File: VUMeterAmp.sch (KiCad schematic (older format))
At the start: 61 parts, among them J1 Conn_01x03, J2 Conn_01x03, J3 Conn_01x07, J4 Conn_01x07, J5 Conn_01x03, SW1 SW_DPST_x2, U1 NJM4580, U2 NJM4580

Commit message: add gbr
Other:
- note added: "+0.4V"
- note added: "-0.4V"
- note added: "4.7k"
- note added: "7.43k\n---\n2.57k"
- note added: "peak cut ±1V"
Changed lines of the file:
@@
 	1    0    0    -1
 $EndComp
+Text Notes 4625 3450 0    50   ~ 0
+7.43k\n---\n2.57k
+Text Notes 7800 3450 0    50   ~ 0
+4.7k
+Text Notes 1950 5275 0    50   ~ 0
+peak cut ±1V
+Text Notes 2175 5850 0    50   ~ 0
++0.4V
+Text Notes 3350 5850 0    50   ~ 0
+-0.4V
 $EndSCHEMATC

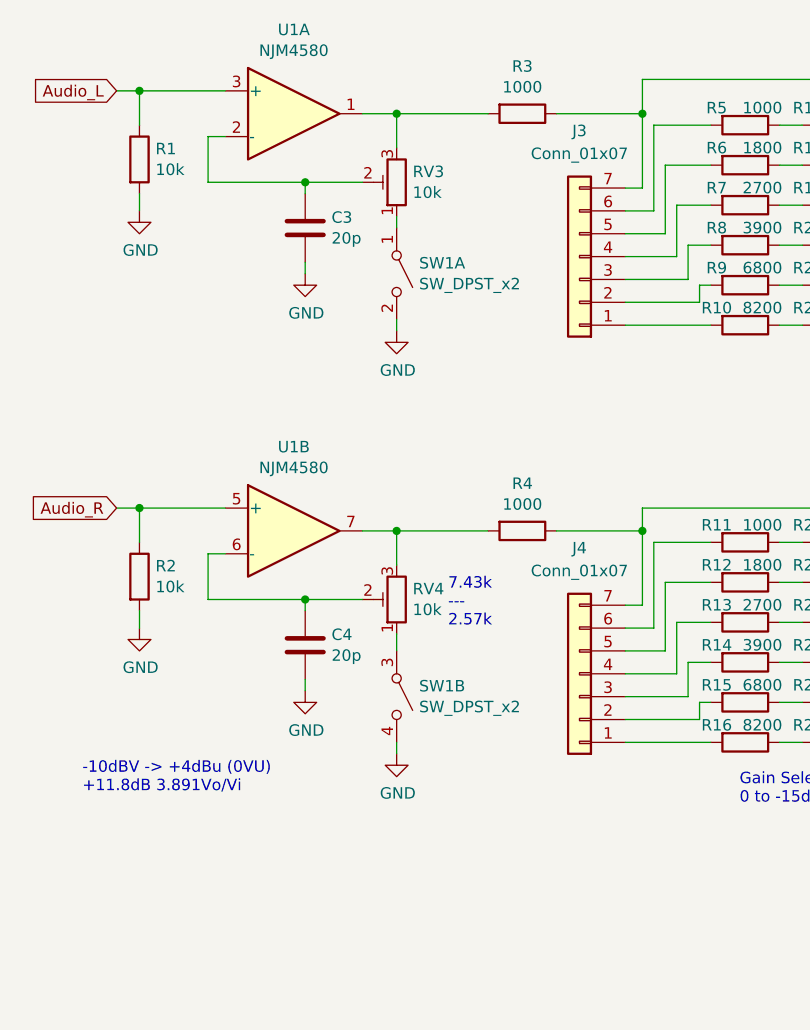
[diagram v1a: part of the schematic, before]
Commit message: delete light
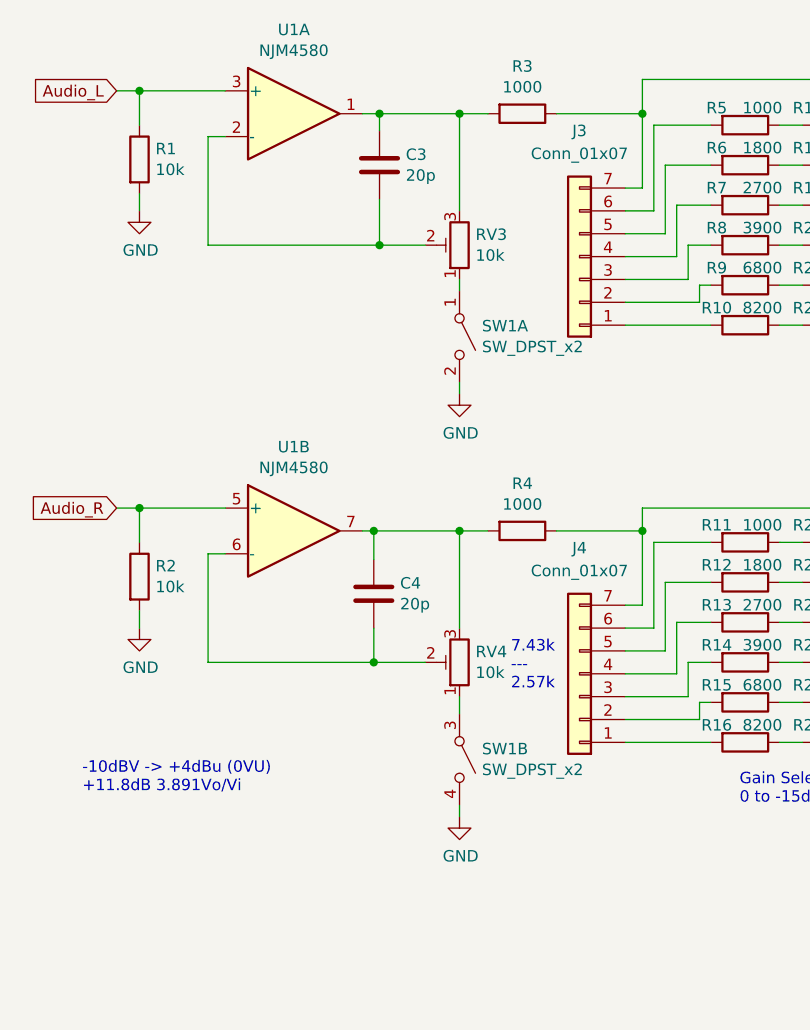
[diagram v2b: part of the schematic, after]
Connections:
- net GND: no longer C3.2, C4.2
- net at R3.2, RV3.3, U1.1: now also C3.1
- net at RV3.2, U1.2 (-): now also C3.2; no longer C3.1
- net at RV4.2, U1.6 (-): now also C4.2; no longer C4.1
- net at R4.2, RV4.3, U1.7: now also C4.1
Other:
- moved on the sheet: C3, C4, RV3, RV4, SW1A, SW1B
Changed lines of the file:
@@
 L Switch:SW_DPST_x2 SW1
 U 1 1 5FF00E09
-P 4400 1900
-F 0 "SW1" V 4354 1998 50  0000 L CNN
-F 1 "SW_DPST_x2" V 4445 1998 50  0000 L CNN
-F 2 "Connector_JST:JST_XH_B4B-XH-A_1x04_P2.50mm_Vertical" H 4400 1900 50  0001 C CNN
-F 3 "~" H 4400 1900 50  0001 C CNN
-	1    4400 1900
+P 4675 2175
+F 0 "SW1" V 4629 2273 50  0000 L CNN
+F 1 "SW_DPST_x2" V 4720 2273 50  0000 L CNN
+F 2 "Connector_JST:JST_XH_B4B-XH-A_1x04_P2.50mm_Vertical" H 4675 2175 50  0001 C CNN
+F 3 "~" H 4675 2175 50  0001 C CNN
+	1    4675 2175
 	0    1    1    0
 $EndComp
@@
 L Device:R_POT_TRIM RV3
 U 1 1 5FF4FE75
-P 4400 1500
-F 0 "RV3" H 4330 1454 50  0000 R CNN
-F 1 "10k" H 4330 1545 50  0000 R CNN
-F 2 "Potentiometer_THT:Potentiometer_Bourns_3296W_Vertical" H 4400 1500 50  0001 C CNN
-F 3 "~" H 4400 1500 50  0001 C CNN
-	1    4400 1500
+P 4675 1775
+F 0 "RV3" H 4605 1729 50  0000 R CNN
+F 1 "10k" H 4605 1820 50  0000 R CNN
+F 2 "Potentiometer_THT:Potentiometer_Bourns_3296W_Vertical" H 4675 1775 50  0001 C CNN
+F 3 "~" H 4675 1775 50  0001 C CNN
+	1    4675 1775
 	-1   0    0    1
 $EndComp
@@
 L power:GND #PWR09
 U 1 1 5FF5A770
-P 4400 2150
-F 0 "#PWR09" H 4400 1900 50  0001 C CNN
-F 1 "GND" H 4405 1977 50  0000 C CNN
-F 2 "" H 4400 2150 50  0001 C CNN
-F 3 "" H 4400 2150 50  0001 C CNN
-	1    4400 2150
-	1    0    0    -1
-$EndComp
-Wire Wire Line
-	4400 1350 4400 1200
-Wire Wire Line
-	4400 1200 4250 1200
+P 4675 2425
+F 0 "#PWR09" H 4675 2175 50  0001 C CNN
+F 1 "GND" H 4680 2252 50  0000 C CNN
+F 2 "" H 4675 2425 50  0001 C CNN
+F 3 "" H 4675 2425 50  0001 C CNN
+	1    4675 2425
+	1    0    0    -1
+$EndComp
+Wire Wire Line
+	4675 1625 4675 1200
+Wire Wire Line
+	4675 1200 4325 1200
 Wire Wire Line
 	3650 1300 3575 1300
-Wire Wire Line
-	3575 1300 3575 1500
-Wire Wire Line
-	3575 1500 4000 1500
 $Comp
 L Device:C C3
 U 1 1 5FF5F53F
-P 4000 1700
-F 0 "C3" H 4115 1746 50  0000 L CNN
-F 1 "20p" H 4115 1655 50  0000 L CNN
-F 2 "Capacitor_SMD:C_0603_1608Metric_Pad1.05x0.95mm_HandSolder" H 4038 1550 50  0001 C CNN
-F 3 "~" H 4000 1700 50  0001 C CNN
-	1    4000 1700
-	1    0    0    -1
-$EndComp
-Wire Wire Line
-	4000 1550 4000 1500
-Connection ~ 4000 1500
-Wire Wire Line
-	4000 1500 4250 1500
-Wire Wire Line
-	4000 1850 4000 1900
+P 4325 1425
+F 0 "C3" H 4440 1471 50  0000 L CNN
+F 1 "20p" H 4440 1380 50  0000 L CNN
+F 2 "Capacitor_SMD:C_0603_1608Metric_Pad1.05x0.95mm_HandSolder" H 4363 1275 50  0001 C CNN
+F 3 "~" H 4325 1425 50  0001 C CNN
+	1    4325 1425
+	1    0    0    -1
+$EndComp
 $Comp
 L Device:R R1
@@
 L Device:R_POT_TRIM RV4
 U 1 1 5FF97E91
-P 4400 3325
-F 0 "RV4" H 4330 3279 50  0000 R CNN
-F 1 "10k" H 4330 3370 50  0000 R CNN
-F 2 "Potentiometer_THT:Potentiometer_Bourns_3296W_Vertical" H 4400 3325 50  0001 C CNN
-F 3 "~" H 4400 3325 50  0001 C CNN
-	1    4400 3325
+P 4675 3600
+F 0 "RV4" H 4605 3554 50  0000 R CNN
+F 1 "10k" H 4605 3645 50  0000 R CNN
+F 2 "Potentiometer_THT:Potentiometer_Bourns_3296W_Vertical" H 4675 3600 50  0001 C CNN
+F 3 "~" H 4675 3600 50  0001 C CNN
+	1    4675 3600
 	-1   0    0    1
 $EndComp
 Wire Wire Line
-	4400 3175 4400 3025
-Wire Wire Line
-	4400 3025 4250 3025
+	4675 3450 4675 3025
+Wire Wire Line
+	4675 3025 4300 3025
 Wire Wire Line
 	3650 3125 3575 3125
-Wire Wire Line
-	3575 3125 3575 3325
-Wire Wire Line
-	3575 3325 4000 3325
 $Comp
 L Device:C C4
 U 1 1 5FF97EAB
-P 4000 3525
-F 0 "C4" H 4115 3571 50  0000 L CNN
-F 1 "20p" H 4115 3480 50  0000 L CNN
-F 2 "Capacitor_SMD:C_0603_1608Metric_Pad1.05x0.95mm_HandSolder" H 4038 3375 50  0001 C CNN
-F 3 "~" H 4000 3525 50  0001 C CNN
-	1    4000 3525
-	1    0    0    -1
-$EndComp
-Wire Wire Line
-	4000 3375 4000 3325
-Connection ~ 4000 3325
-Wire Wire Line
-	4000 3325 4250 3325
-Wire Wire Line
-	4000 3675 4000 3725
+P 4300 3300
+F 0 "C4" H 4415 3346 50  0000 L CNN
+F 1 "20p" H 4415 3255 50  0000 L CNN
+F 2 "Capacitor_SMD:C_0603_1608Metric_Pad1.05x0.95mm_HandSolder" H 4338 3150 50  0001 C CNN
+F 3 "~" H 4300 3300 50  0001 C CNN
+	1    4300 3300
+	1    0    0    -1
+$EndComp
 $Comp
 L Device:R R2
@@
 	3175 2925 3275 2925
 Connection ~ 3275 2925
-$Comp
-L power:GND #PWR07
-U 1 1 5FFA78F7
-P 4000 1900
-F 0 "#PWR07" H 4000 1650 50  0001 C CNN
-F 1 "GND" H 4005 1727 50  0000 C CNN
-F 2 "" H 4000 1900 50  0001 C CNN
-F 3 "" H 4000 1900 50  0001 C CNN
-	1    4000 1900
-	1    0    0    -1
-$EndComp
-$Comp
-L power:GND #PWR08
-U 1 1 5FFA9D24
-P 4000 3725
-F 0 "#PWR08" H 4000 3475 50  0001 C CNN
-F 1 "GND" H 4005 3552 50  0000 C CNN
-F 2 "" H 4000 3725 50  0001 C CNN
-F 3 "" H 4000 3725 50  0001 C CNN
-	1    4000 3725
-	1    0    0    -1
-$EndComp
-Wire Wire Line
-	4400 2150 4400 2100
-Wire Wire Line
-	4400 1700 4400 1650
+Wire Wire Line
+	4675 2425 4675 2375
+Wire Wire Line
+	4675 1975 4675 1925
 $Comp
 L Switch:SW_DPST_x2 SW1
 U 2 1 5FFC5DD0
-P 4400 3750
-F 0 "SW1" V 4354 3848 50  0000 L CNN
-F 1 "SW_DPST_x2" V 4445 3848 50  0000 L CNN
-F 2 "Connector_JST:JST_XH_B4B-XH-A_1x04_P2.50mm_Vertical" H 4400 3750 50  0001 C CNN
-F 3 "~" H 4400 3750 50  0001 C CNN
-	2    4400 3750
+P 4675 4025
+F 0 "SW1" V 4629 4123 50  0000 L CNN
+F 1 "SW_DPST_x2" V 4720 4123 50  0000 L CNN
+F 2 "Connector_JST:JST_XH_B4B-XH-A_1x04_P2.50mm_Vertical" H 4675 4025 50  0001 C CNN
+F 3 "~" H 4675 4025 50  0001 C CNN
+	2    4675 4025
 	0    1    1    0
 $EndComp
@@
 L power:GND #PWR010
 U 1 1 5FFC5DDA
-P 4400 4000
-F 0 "#PWR010" H 4400 3750 50  0001 C CNN
-F 1 "GND" H 4405 3827 50  0000 C CNN
-F 2 "" H 4400 4000 50  0001 C CNN
-F 3 "" H 4400 4000 50  0001 C CNN
-	1    4400 4000
-	1    0    0    -1
-$EndComp
-Wire Wire Line
-	4400 4000 4400 3950
-Wire Wire Line
-	4400 3475 4400 3550
+P 4675 4275
+F 0 "#PWR010" H 4675 4025 50  0001 C CNN
+F 1 "GND" H 4680 4102 50  0000 C CNN
+F 2 "" H 4675 4275 50  0001 C CNN
+F 3 "" H 4675 4275 50  0001 C CNN
+	1    4675 4275
+	1    0    0    -1
+$EndComp
+Wire Wire Line
+	4675 4275 4675 4225
+Wire Wire Line
+	4675 3750 4675 3825
 $Comp
 L Connector_Generic:Conn_01x07 J3
@@
 $EndComp
 Wire Wire Line
-	4800 1200 4400 1200
-Connection ~ 4400 1200
+	4800 1200 4675 1200
+Connection ~ 4675 1200
 Wire Wire Line
 	5100 1200 5475 1200
@@
 Connection ~ 6575 3250
 Wire Wire Line
-	4800 3025 4400 3025
-Connection ~ 4400 3025
+	4800 3025 4675 3025
+Connection ~ 4675 3025
 Text GLabel 1625 2300 2    50   Input ~ 0
 Audio_L
@@
 	1    0    0    -1
 $EndComp
-Text Notes 4625 3450 0    50   ~ 0
+Text Notes 4900 3725 0    50   ~ 0
 7.43k\n---\n2.57k
 Text Notes 7800 3450 0    50   ~ 0
@@
 Text Notes 3350 5850 0    50   ~ 0
 -0.4V
+Wire Wire Line
+	4525 1775 4325 1775
+Wire Wire Line
+	4325 1775 4325 1575
+Wire Wire Line
+	4325 1275 4325 1200
+Connection ~ 4325 1200
+Wire Wire Line
+	4325 1200 4250 1200
+Wire Wire Line
+	4325 1775 3575 1775
+Wire Wire Line
+	3575 1300 3575 1775
+Connection ~ 4325 1775
+Wire Wire Line
+	4300 3150 4300 3025
+Connection ~ 4300 3025
+Wire Wire Line
+	4300 3025 4250 3025
+Wire Wire Line
+	4300 3450 4300 3600
+Wire Wire Line
+	4300 3600 4525 3600
+Wire Wire Line
+	3575 3125 3575 3600
+Wire Wire Line
+	3575 3600 4300 3600
+Connection ~ 4300 3600
 $EndSCHEMATC
